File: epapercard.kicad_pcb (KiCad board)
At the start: 2 copper layers, 88.9 x 50.8 mm, 44 parts, among them P1 PROG, P2 A120699CT, Q1 2N7002KW, Q2 BSS84W, Q3 BSS84W, Q4 BSS84W, Q5 2N7002KW, Q6 2N7002KW, Q7 2N7002KW, SW1 SW_PUSH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

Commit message: Changed battery footprint
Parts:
- removed BT2: CR2032, footprint:CR2032sm
- removed G***: LOGO, footprint:oshlogo
- BT1: value CR2032 -> CR2016; footprint footprint:CR2032sm -> footprint:CR2016sm
- P1: value PROG -> CONN_01X06
- moved BT1 10.2 mm to (51.8, 42.2)
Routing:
- net +3V3: track 162.0 -> 112.5 mm
- net GND: track 65.1 -> 46.3 mm, vias 14 -> 13
- net SPI_CLK: track 54.0 -> 54.7 mm

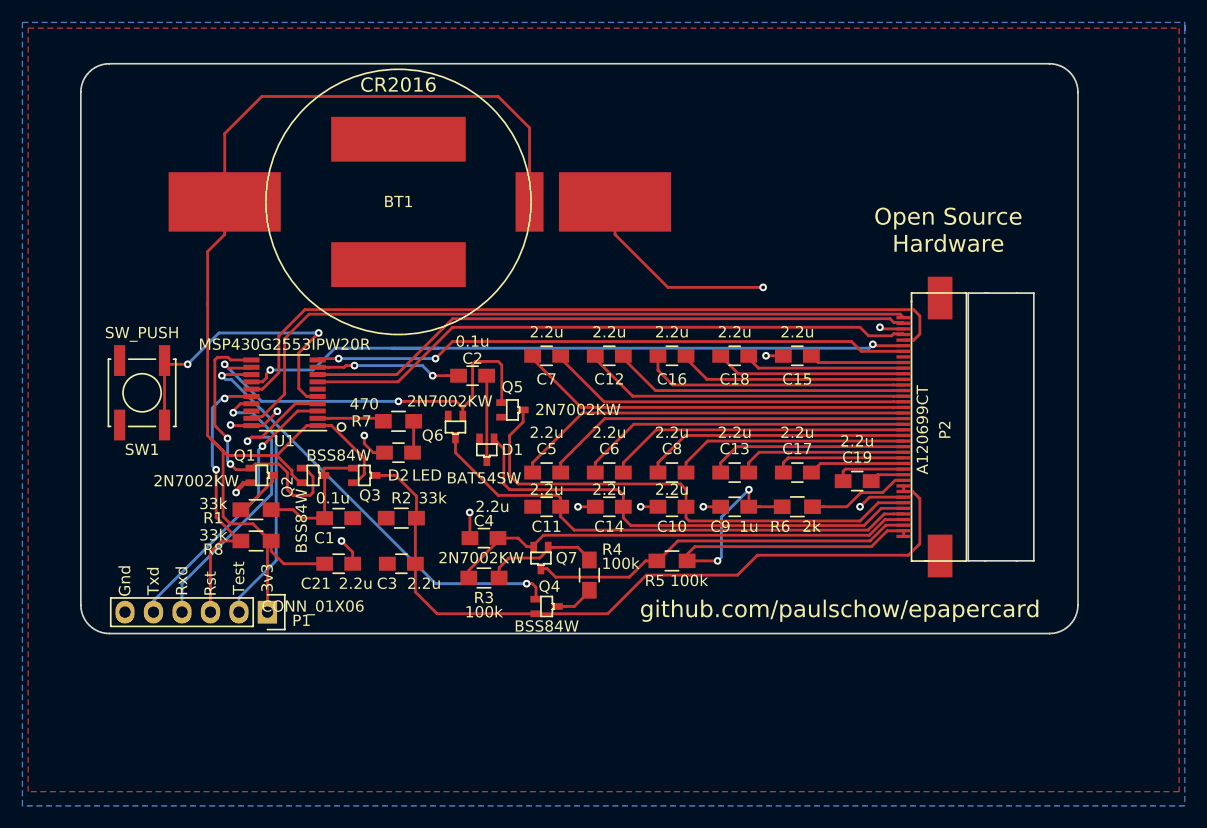
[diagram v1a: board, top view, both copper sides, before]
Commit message: Adjusted dimensions
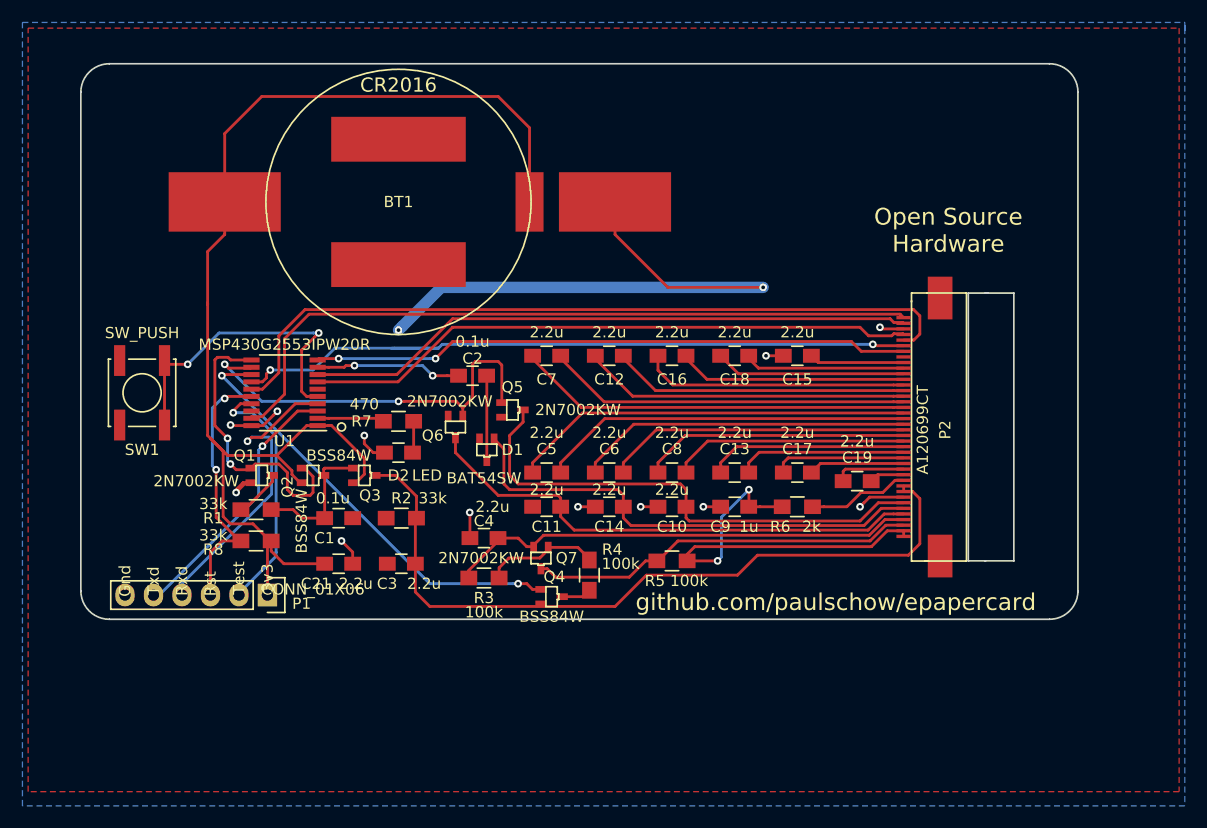
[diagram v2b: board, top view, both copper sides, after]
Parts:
- moved P1 1.52 mm to (40.1, 77.2)
- moved Q4 0.98 mm to (65.5, 77.4)
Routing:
- net GND: track 46.3 -> 80.4 mm, vias 13 -> 14
- net /test: track 23.8 -> 22.3 mm
- net /rxd: track 28.8 -> 27.3 mm
- net +3V3: track 112.5 -> 111.0 mm
- net /rst: track 25.3 -> 23.8 mm
- net /txd: track 25.0 -> 24.0 mm
- net Net-(Q4-Pad3): track 3.52 -> 2.75 mm
- net BORDER_CONTROL: track 39.6 -> 39.0 mm
- net +3.3VP: track 67.6 -> 67.1 mm
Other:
- board size 88.9 x 50.8 mm -> 88.9 x 49.5 mm

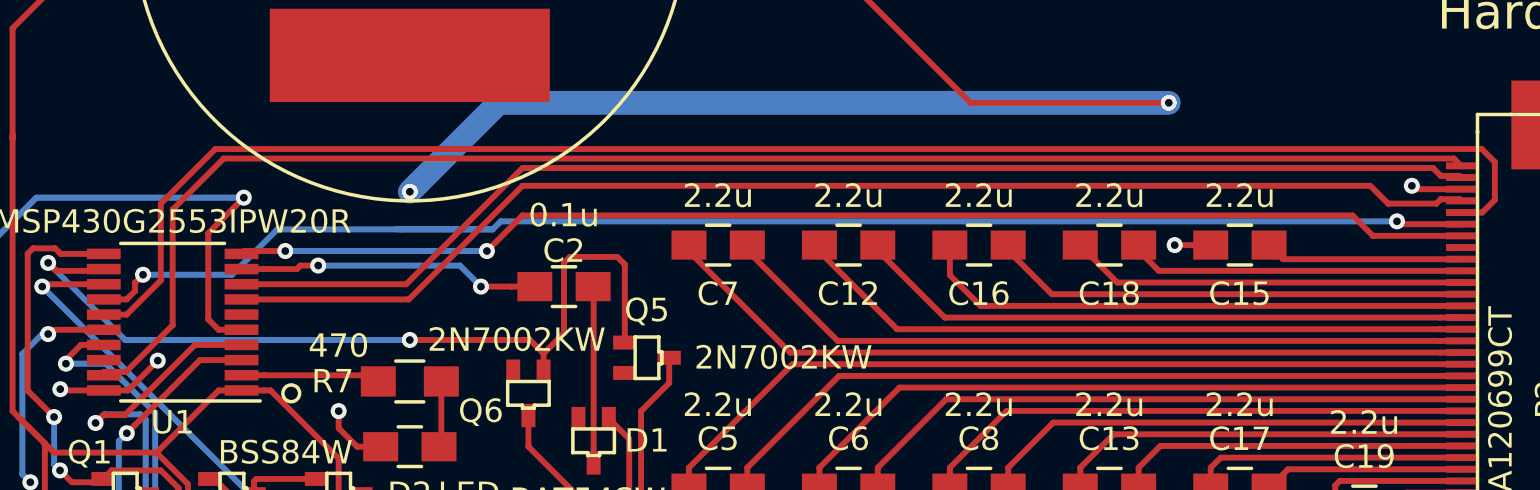
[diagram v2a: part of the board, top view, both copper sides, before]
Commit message: Added boost regulator
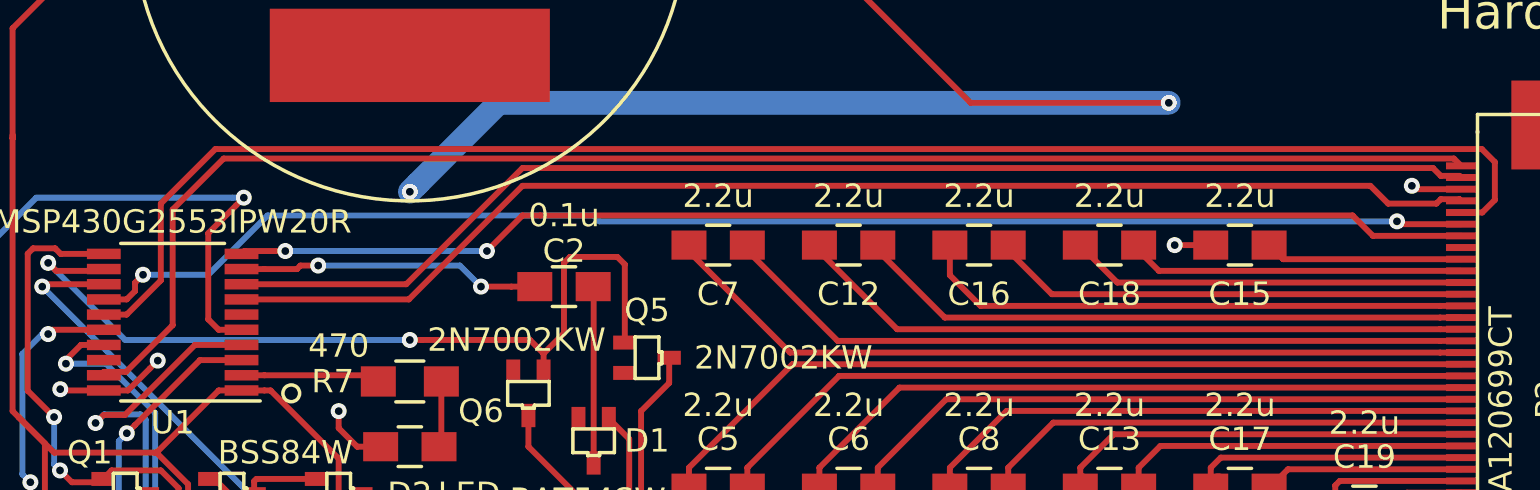
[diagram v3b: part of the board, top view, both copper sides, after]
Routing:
- net SPI_MISO: track 63.9 -> 60.0 mm
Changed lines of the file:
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@@
     (links 103)
     (no_connects 1)
-    (area 23.419999 29.769999 112.470001 80.720001)
+    (area 18.288 26.162 121.920001 96.012001)
     (thickness 1.6)
     (drawings 26)
-    (tracks 454)
+    (tracks 452)
     (zones 0)
     (modules 42)
@@
   (segment (start 41.148 57.394) (end 39.685 58.857) (width 0.254) (layer F.Cu) (net 41))
   (segment (start 39.685 58.857) (end 38.706 58.857) (width 0.254) (layer F.Cu) (net 41))
-  (segment (start 55.372 55.204579) (end 55.712579 54.864) (width 0.254) (layer B.Cu) (net 42))
-  (segment (start 55.712579 54.864) (end 94.102181 54.864) (width 0.254) (layer B.Cu) (net 42))
-  (segment (start 94.102181 54.864) (end 94.104501 54.86168) (width 0.254) (layer B.Cu) (net 42))
-  (segment (start 55.372 55.204579) (end 46.141421 55.204579) (width 0.254) (layer B.Cu) (net 42))
-  (segment (start 46.141421 55.204579) (end 44.196 57.15) (width 0.254) (layer B.Cu) (net 42))
-  (segment (start 44.196 57.15) (end 40.386 57.15) (width 0.254) (layer B.Cu) (net 42))
+  (segment (start 94.104501 54.86168) (end 94.102181 54.864) (width 0.254) (layer B.Cu) (net 42))
+  (segment (start 94.102181 54.864) (end 59.944 54.864) (width 0.254) (layer B.Cu) (net 42))
+  (segment (start 59.69 54.61) (end 45.72 54.61) (width 0.254) (layer B.Cu) (net 42))
+  (segment (start 59.944 54.864) (end 59.69 54.61) (width 0.254) (layer B.Cu) (net 42))
+  (segment (start 43.18 57.15) (end 40.386 57.15) (width 0.254) (layer B.Cu) (net 42))
+  (segment (start 45.72 54.61) (end 43.18 57.15) (width 0.254) (layer B.Cu) (net 42))
   (segment (start 94.226821 54.984) (end 94.104501 54.86168) (width 0.254) (layer F.Cu) (net 42))
   (segment (start 96.854 54.984) (end 94.226821 54.984) (width 0.254) (layer F.Cu) (net 42))
@@
   (segment (start 39.685 58.207) (end 38.706 58.207) (width 0.254) (layer F.Cu) (net 42))
   (via (at 40.386 57.15) (size 0.6858) (drill 0.3302) (layers F.Cu B.Cu) (net 42))
-  (segment (start 51.475421 55.204579) (end 55.372 55.204579) (width 0.254) (layer B.Cu) (net 42))
-  (segment (start 51.475421 55.204579) (end 51.221421 55.204579) (width 0.254) (layer B.Cu) (net 42))
   (segment (start 56.642 54.61) (end 55.118 56.134) (width 0.254) (layer F.Cu) (net 43))
   (segment (start 57.404 54.61) (end 56.642 54.61) (width 0.254) (layer F.Cu) (net 43))
@@
     (min_thickness 0.254)
     (keepout (tracks not_allowed) (vias not_allowed) (copperpour not_allowed))
-    (fill (arc_segments 16) (thermal_gap 1.27) (thermal_bridge_width 1.27))
+    (fill yes (arc_segments 16) (thermal_gap 1.27) (thermal_bridge_width 1.27))
     (polygon
       (pts
@@
     (min_thickness 0.254)
     (keepout (tracks not_allowed) (vias not_allowed) (copperpour not_allowed))
-    (fill (arc_segments 16) (thermal_gap 1.27) (thermal_bridge_width 1.27))
+    (fill yes (arc_segments 16) (thermal_gap 1.27) (thermal_bridge_width 1.27))
     (polygon
       (pts

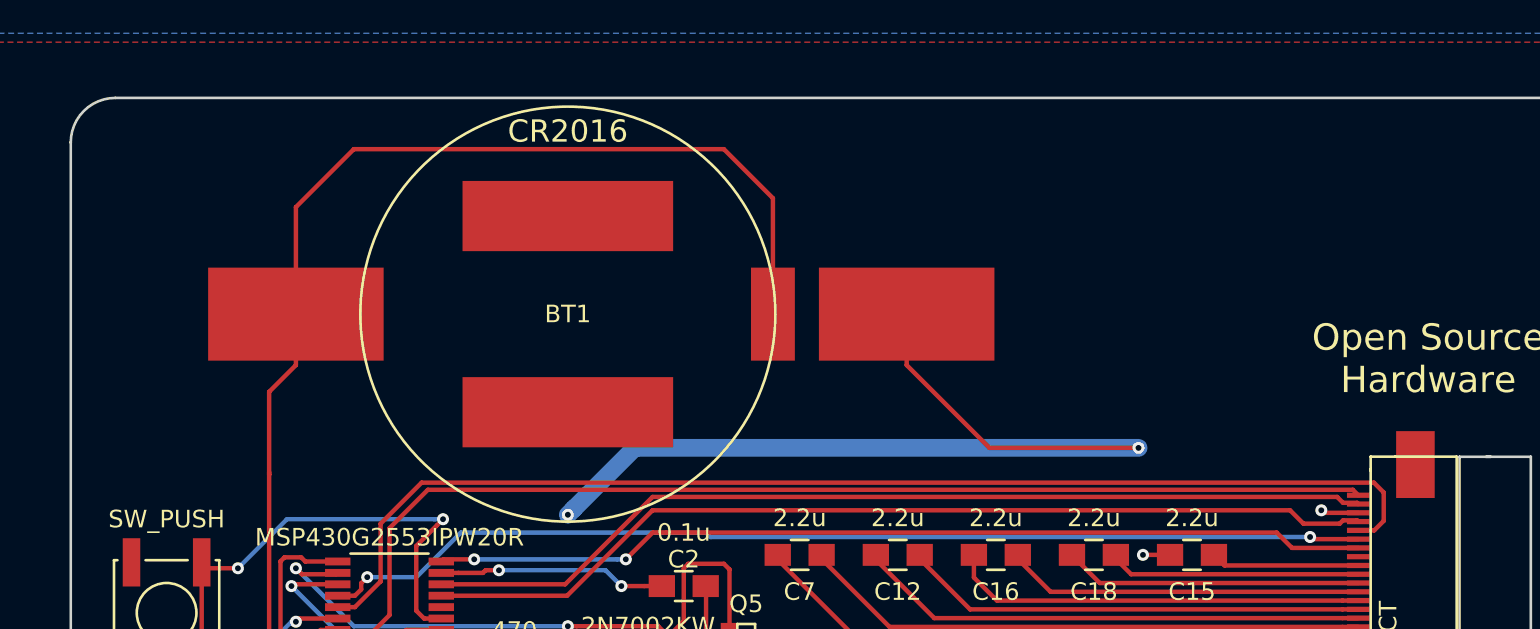
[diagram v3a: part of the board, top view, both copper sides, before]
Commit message: Add tabbed battery and boost reg
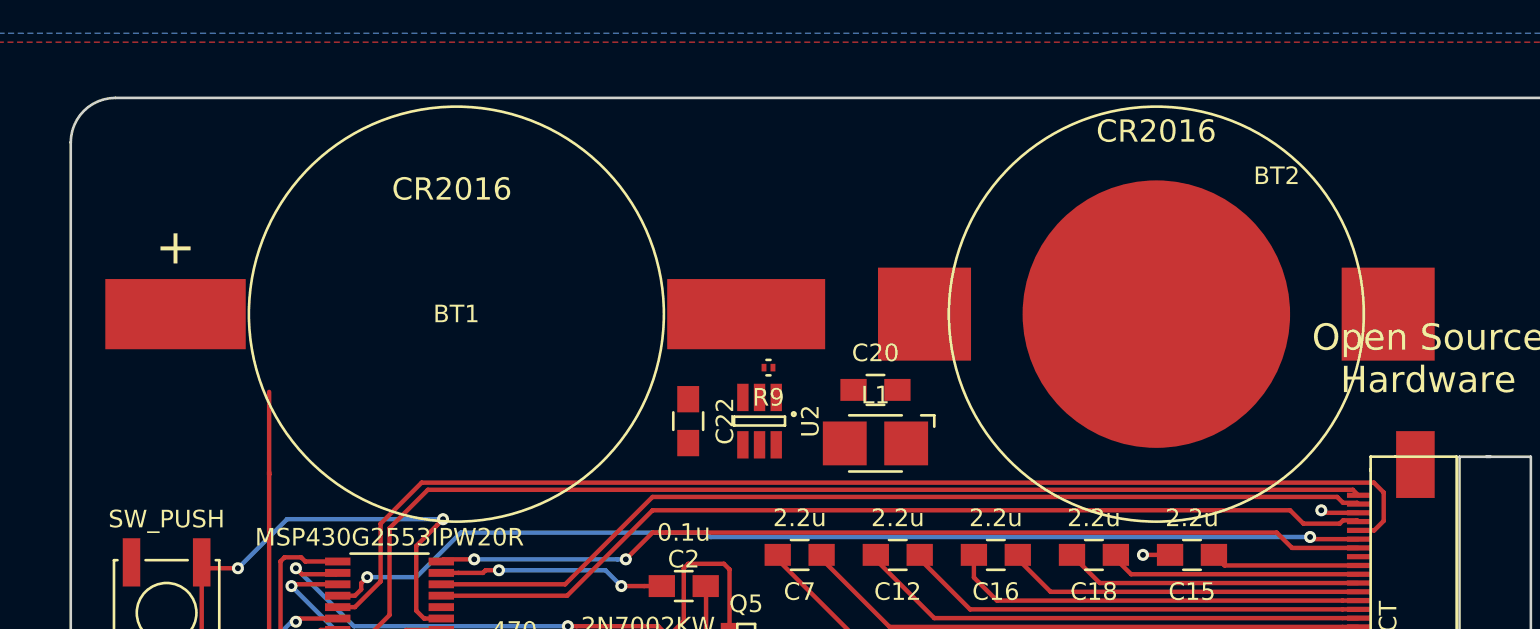
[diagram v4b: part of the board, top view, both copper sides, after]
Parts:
- added BT2: CR2016, footprint:CR2032sm, F.Cu at (85.3, 42.2)
- added C20: 10u, Capacitors_SMD:C_0805_HandSoldering, F.Cu at (69.3, 46.5)
- added C22: 10u, Capacitors_SMD:C_0805_HandSoldering, F.Cu at (58.7, 48.3)
- added L1: 4.7uH, Inductors:Inductor_1212, F.Cu at (69.3, 49.5)
- added R9: DNI, Resistors_SMD:R_0201, F.Cu at (63.2, 45.2)
- added U2: TLV61225, TO_SOT_Packages_SMD:SOT-23-6_Handsoldering, F.Cu at (62.7, 48.3)
- BT1: footprint footprint:CR2016sm -> footprint:CR2016sm-F2N
- moved BT1 6.35 mm to (45.5, 42.2)
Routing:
- net GND: track 80.4 -> 28.2 mm, vias 14 -> 12
- net +3V3: track 111.0 -> 63.5 mm

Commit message: Move a few tracks around
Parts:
- BT1: value CR2016 -> CR2016/F2N
- P1: value CONN_01X06 -> Prog
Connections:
- Q2 pad 2: +3V3 -> /Vboost
- Q3 pad 2: +3V3 -> /Vboost
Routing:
- net +3V3: track 63.5 -> 153.0 mm
- net /Vboost: track 0.00 -> 16.0 mm, vias 0 -> 2
- net SPI_MISO: track 60.0 -> 60.5 mm

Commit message: Everything connected
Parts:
- removed R9: DNI, Resistors_SMD:R_0201
- BT1: value CR2016/F2N -> CR2016
- P1: value Prog -> PROG
- U2: footprint TO_SOT_Packages_SMD:SOT-23-6_Handsoldering -> TO_SOT_Packages_SMD:SOT-23-6
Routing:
- net /Vboost: track 16.0 -> 50.1 mm, vias 2 -> 3
- net /led: track 5.99 -> 28.7 mm, vias 0 -> 2
- net +3V3: track 153.0 -> 164.9 mm
- net GND: track 28.2 -> 37.0 mm, vias 12 -> 14
- net Net-(L1-Pad2): track 0.00 -> 6.44 mm
- net +3.3VP: track 67.1 -> 68.7 mm
